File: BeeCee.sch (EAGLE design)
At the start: 0 parts

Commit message: finalized USB C & AB connectors
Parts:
- added K1: (no value), Eagle_INPUT_OUTPUT_CONNECTORS_rev15d:629105150921
- added U$1: (no value), Eagle_INPUT_OUTPUT_CONNECTORS_rev15d:632712000011(T)
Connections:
- new net CC: U$1.CC1
- new net GND: U$1.GND, U$1.GND1, U$1.GND2, U$1.GND3
- new net VCC: U$1.VBUS, U$1.VBUS1, U$1.VBUS2, U$1.VBUS3
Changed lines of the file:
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@@
 <grid distance="0.1" unitdist="inch" unit="inch" style="lines" multiple="1" display="no" altdistance="0.01" altunitdist="inch" altunit="inch"/>
 <layers>
+<layer number="1" name="Top" color="4" fill="1" visible="no" active="no"/>
+<layer number="16" name="Bottom" color="1" fill="1" visible="no" active="no"/>
+<layer number="17" name="Pads" color="2" fill="1" visible="no" active="no"/>
+<layer number="18" name="Vias" color="2" fill="1" visible="no" active="no"/>
+<layer number="19" name="Unrouted" color="6" fill="1" visible="no" active="no"/>
+<layer number="20" name="Dimension" color="15" fill="1" visible="no" active="no"/>
+<layer number="21" name="tPlace" color="13" fill="1" visible="no" active="no"/>
+<layer number="22" name="bPlace" color="7" fill="1" visible="no" active="no"/>
+<layer number="23" name="tOrigins" color="15" fill="1" visible="no" active="no"/>
+<layer number="24" name="bOrigins" color="15" fill="1" visible="no" active="no"/>
+<layer number="25" name="tNames" color="2" fill="1" visible="no" active="no"/>
+<layer number="26" name="bNames" color="7" fill="1" visible="no" active="no"/>
+<layer number="27" name="tValues" color="11" fill="1" visible="no" active="no"/>
+<layer number="28" name="bValues" color="7" fill="1" visible="no" active="no"/>
+<layer number="29" name="tStop" color="7" fill="3" visible="no" active="no"/>
+<layer number="30" name="bStop" color="7" fill="6" visible="no" active="no"/>
+<layer number="31" name="tCream" color="7" fill="4" visible="no" active="no"/>
+<layer number="32" name="bCream" color="7" fill="5" visible="no" active="no"/>
+<layer number="33" name="tFinish" color="6" fill="3" visible="no" active="no"/>
+<layer number="34" name="bFinish" color="6" fill="6" visible="no" active="no"/>
+<layer number="35" name="tGlue" color="7" fill="4" visible="no" active="no"/>
+<layer number="36" name="bGlue" color="7" fill="5" visible="no" active="no"/>
+<layer number="37" name="tTest" color="7" fill="1" visible="no" active="no"/>
+<layer number="38" name="bTest" color="7" fill="1" visible="no" active="no"/>
+<layer number="39" name="tKeepout" color="4" fill="11" visible="no" active="no"/>
+<layer number="40" name="bKeepout" color="1" fill="11" visible="no" active="no"/>
+<layer number="41" name="tRestrict" color="4" fill="10" visible="no" active="no"/>
+<layer number="42" name="bRestrict" color="1" fill="10" visible="no" active="no"/>
+<layer number="43" name="vRestrict" color="2" fill="10" visible="no" active="no"/>
+<layer number="44" name="Drills" color="7" fill="1" visible="no" active="no"/>
+<layer number="45" name="Holes" color="7" fill="1" visible="no" active="no"/>
+<layer number="46" name="Milling" color="3" fill="1" visible="no" active="no"/>
+<layer number="47" name="Measures" color="7" fill="1" visible="no" active="no"/>
+<layer number="48" name="Document" color="7" fill="1" visible="no" active="no"/>
+<layer number="49" name="Reference" color="7" fill="1" visible="no" active="no"/>
+<layer number="50" name="dxf" color="7" fill="1" visible="no" active="no"/>
+<layer number="51" name="tDocu" color="14" fill="1" visible="no" active="no"/>
+<layer number="52" name="bDocu" color="7" fill="1" visible="no" active="no"/>
 <layer number="90" name="Modules" color="5" fill="1" visible="yes" active="yes"/>
 <layer number="91" name="Nets" color="2" fill="1" visible="yes" active="yes"/>
@@
 <layer number="97" name="Info" color="7" fill="1" visible="yes" active="yes"/>
 <layer number="98" name="Guide" color="6" fill="1" visible="yes" active="yes"/>
+<layer number="250" name="Descript" color="7" fill="1" visible="yes" active="yes"/>
+<layer number="251" name="SMDround" color="7" fill="1" visible="yes" active="yes"/>
 </layers>
 <schematic xreflabel="%F%N/%S.%C%R" xrefpart="/%S.%C%R">
@@
 </classes>
 <parts>
+<part name="U$1" library="Eagle_INPUT_OUTPUT_CONNECTORS_rev15d" deviceset="632712000011" device="(T)"/>
+<part name="K1" library="Eagle_INPUT_OUTPUT_CONNECTORS_rev15d" deviceset="629105150921" device=""/>
+<part name="GND1" library="supply1" deviceset="GND" device=""/>
+<part name="GND2" library="supply1" deviceset="GND" device=""/>
+<part name="GND3" library="supply1" deviceset="GND" device=""/>
+<part name="GND4" library="supply1" deviceset="GND" device=""/>
+<part name="P+1" library="supply1" deviceset="VCC" device=""/>
+<part name="P+2" library="supply1" deviceset="VCC" device=""/>
+<part name="P+3" library="supply1" deviceset="VCC" device=""/>
+<part name="P+4" library="supply1" deviceset="VCC" device=""/>
 </parts>
 <sheets>
@@
 </plain>
 <instances>
+<instance part="U$1" gate="G$1" x="53.34" y="58.42"/>
+<instance part="K1" gate="G$1" x="144.78" y="58.42"/>
+<instance part="GND1" gate="1" x="5.08" y="66.04"/>
+<instance part="GND2" gate="1" x="5.08" y="38.1"/>
+<instance part="GND3" gate="1" x="55.88" y="38.1" smashed="yes">
+<attribute name="VALUE" x="53.34" y="35.56" size="1.778" layer="96"/>
+</instance>
+<instance part="GND4" gate="1" x="55.88" y="66.04" smashed="yes">
+<attribute name="VALUE" x="53.34" y="63.5" size="1.778" layer="96"/>
+</instance>
+<instance part="P+1" gate="VCC" x="15.24" y="63.5"/>
+<instance part="P+2" gate="VCC" x="50.8" y="63.5"/>
+<instance part="P+3" gate="VCC" x="15.24" y="50.8"/>
+<instance part="P+4" gate="VCC" x="55.88" y="50.8"/>
 </instances>
 <busses>
 </busses>
 <nets>
+<net name="GND" class="0">
+<segment>
+<pinref part="U$1" gate="G$1" pin="GND"/>
+<pinref part="GND1" gate="1" pin="GND"/>
+<wire x1="20.32" y1="68.58" x2="5.08" y2="68.58" width="0.1524" layer="91"/>
+</segment>
+<segment>
+<pinref part="U$1" gate="G$1" pin="GND1"/>
+<pinref part="GND2" gate="1" pin="GND"/>
+<wire x1="20.32" y1="40.64" x2="5.08" y2="40.64" width="0.1524" layer="91"/>
+</segment>
+<segment>
+<pinref part="GND3" gate="1" pin="GND"/>
+<pinref part="U$1" gate="G$1" pin="GND3"/>
+<wire x1="55.88" y1="40.64" x2="59.69" y2="40.64" width="0.1524" layer="91"/>
+</segment>
+<segment>
+<pinref part="U$1" gate="G$1" pin="GND2"/>
+<pinref part="GND4" gate="1" pin="GND"/>
+<wire x1="59.69" y1="68.58" x2="55.88" y2="68.58" width="0.1524" layer="91"/>
+</segment>
+</net>
+<net name="VCC" class="0">
+<segment>
+<pinref part="P+1" gate="VCC" pin="VCC"/>
+<pinref part="U$1" gate="G$1" pin="VBUS"/>
+<wire x1="15.24" y1="60.96" x2="20.32" y2="60.96" width="0.1524" layer="91"/>
+<wire x1="15.24" y1="60.96" x2="20.32" y2="60.96" width="0.1524" layer="91"/>
+</segment>
+<segment>
+<pinref part="P+3" gate="VCC" pin="VCC"/>
+<pinref part="U$1" gate="G$1" pin="VBUS1"/>
+<wire x1="15.24" y1="48.26" x2="20.32" y2="48.26" width="0.1524" layer="91"/>
+</segment>
+<segment>
+<pinref part="U$1" gate="G$1" pin="VBUS2"/>
+<pinref part="P+2" gate="VCC" pin="VCC"/>
+<wire x1="59.69" y1="60.96" x2="50.8" y2="60.96" width="0.1524" layer="91"/>
+</segment>
+<segment>
+<pinref part="U$1" gate="G$1" pin="VBUS3"/>
+<pinref part="P+4" gate="VCC" pin="VCC"/>
+<wire x1="59.69" y1="48.26" x2="55.88" y2="48.26" width="0.1524" layer="91"/>
+</segment>
+</net>
+<net name="CC" class="0">
+<segment>
+<pinref part="U$1" gate="G$1" pin="CC1"/>
+<wire x1="20.32" y1="58.42" x2="15.24" y2="58.42" width="0.1524" layer="91"/>
+<label x="15.24" y="58.42" size="1.778" layer="95" rot="R180" xref="yes"/>
+</segment>
+</net>
 </nets>
 </sheet>

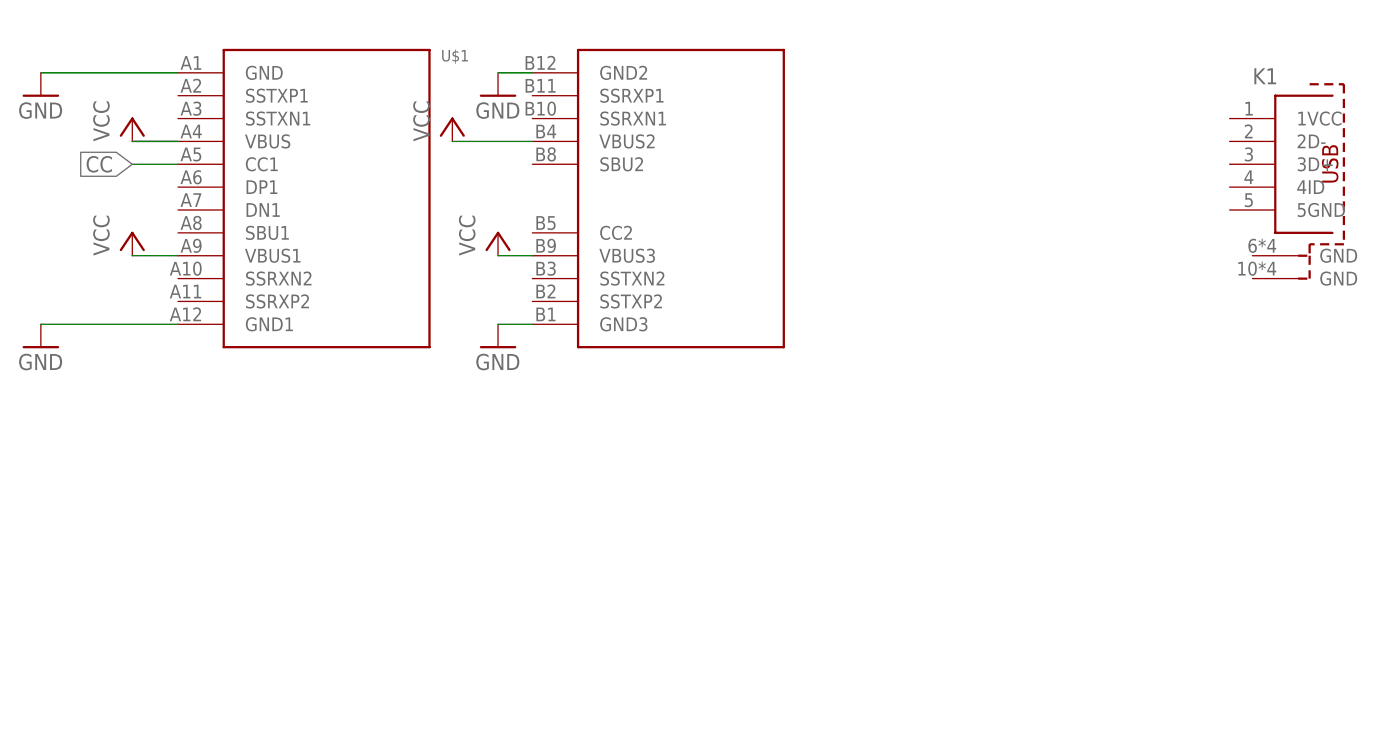
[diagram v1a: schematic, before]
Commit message: finished up the schematics, gave up on finding a small enough selector switch
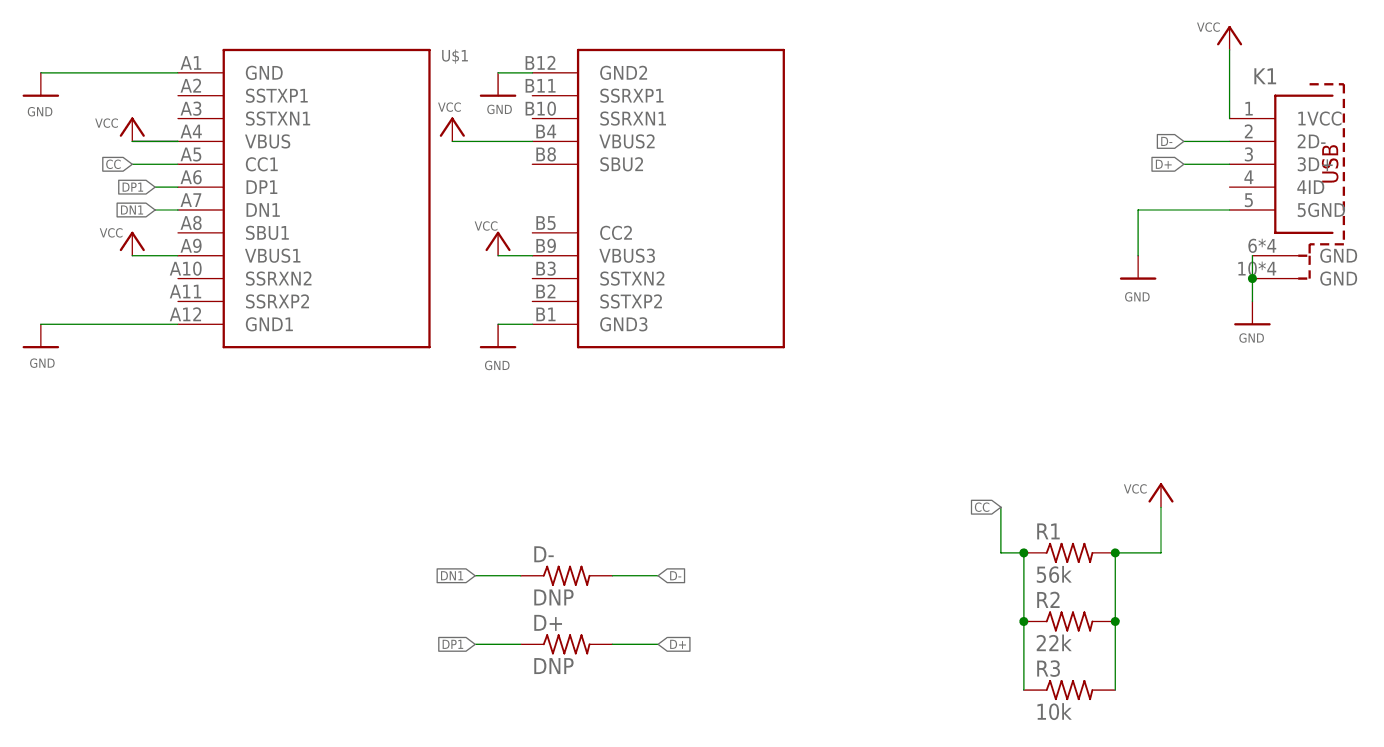
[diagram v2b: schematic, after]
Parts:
- added D+, D-: DNP, adafruit:R-US_R0805
- added R1: 56k, adafruit:R-US_R0805
- added R2: 22k, adafruit:R-US_R0805
- added R3: 10k, adafruit:R-US_R0805
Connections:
- new net D+: D+.2, K1.3D+
- new net D-: D-.2, K1.2D-
- new net DN1: D-.1, U$1.DN1
- new net DP1: D+.1, U$1.DP1
- net CC: now also R1.1, R2.1, R3.1
- net GND: now also K1.5GND, K1.GND@1, K1.GND@2
- net VCC: now also K1.1VCC, R1.2, R2.2, R3.2

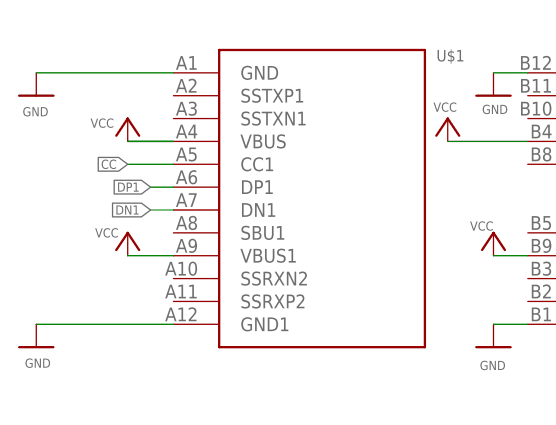
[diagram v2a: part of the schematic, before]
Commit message: preliminary component layout. Might be able to squeeze in a selector switch
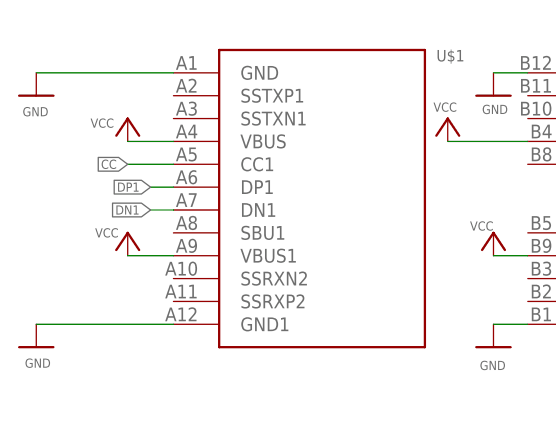
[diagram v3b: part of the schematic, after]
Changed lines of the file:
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@@
 <pinref part="U$1" gate="G$1" pin="VBUS"/>
-<wire x1="15.24" y1="60.96" x2="20.32" y2="60.96" width="0.1524" layer="91"/>
 <wire x1="15.24" y1="60.96" x2="20.32" y2="60.96" width="0.1524" layer="91"/>
 </segment>
